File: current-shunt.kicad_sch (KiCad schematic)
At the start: 22 parts, among them J1 Conn_01x02, U1 TSR_1-2450

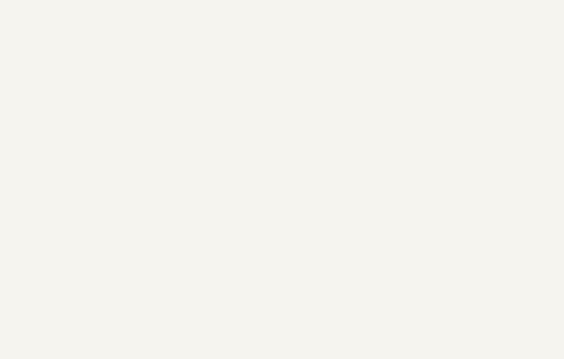
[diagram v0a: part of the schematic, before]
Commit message: Add License to repo and board
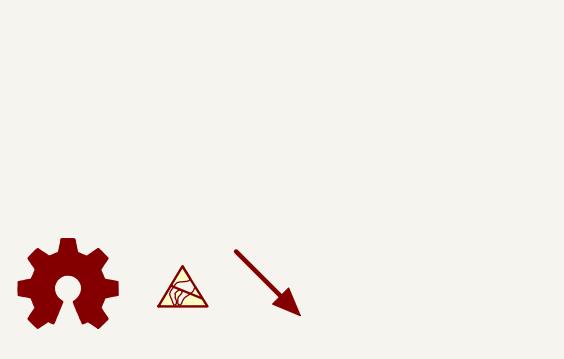
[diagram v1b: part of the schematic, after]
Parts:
- added LOGO1: Logo_Open_Hardware_Small, Symbol:OSHW-Logo2_14.6x12mm_SilkScreen, symbol Graphic:Logo_Open_Hardware_Small
- added LOGO2: SYM_ESD_Small, Symbol:ESD-Logo_6.6x6mm_SilkScreen, symbol Graphic:SYM_ESD_Small
- added LOGO3: SYM_Arrow45_XLarge, Symbol:KiCad-Logo2_5mm_SilkScreen, symbol Graphic:SYM_Arrow45_XLarge
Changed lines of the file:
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@@
     (pin "2")
+  )
+  (symbol (lib_id "Graphic:SYM_ESD_Small") (at 36.83 186.055 0) (unit 1)
+    (in_bom yes) (on_board yes) (fields_autoplaced)
+    (property "Reference" "LOGO2" (id 0) (at 36.83 182.499 0)
+      (effects (font (size 1.27 1.27)) hide)
+    )
+    (property "Value" "SYM_ESD_Small" (id 1) (at 36.83 189.23 0)
+      (effects (font (size 1.27 1.27)) hide)
+    )
+    (property "Footprint" "Symbol:ESD-Logo_6.6x6mm_SilkScreen" (id 2) (at 36.83 185.801 0)
+      (effects (font (size 1.27 1.27)) hide)
+    )
+    (property "Datasheet" "~" (id 3) (at 36.83 185.801 0)
+      (effects (font (size 1.27 1.27)) hide)
+    )
   )
   (symbol (lib_id "power:GND") (at 166.37 170.18 0) (unit 1)
@@
     (pin "1")
   )
+  (symbol (lib_id "Graphic:SYM_Arrow45_XLarge") (at 46.355 185.42 0) (unit 1)
+    (in_bom yes) (on_board yes) (fields_autoplaced)
+    (property "Reference" "LOGO3" (id 0) (at 49.149 182.88 0)
+      (effects (font (size 1.27 1.27)) hide)
+    )
+    (property "Value" "SYM_Arrow45_XLarge" (id 1) (at 46.355 189.992 0)
+      (effects (font (size 1.27 1.27)) hide)
+    )
+    (property "Footprint" "Symbol:KiCad-Logo2_5mm_SilkScreen" (id 2) (at 46.355 185.42 0)
+      (effects (font (size 1.27 1.27)) hide)
+    )
+    (property "Datasheet" "~" (id 3) (at 46.355 185.42 0)
+      (effects (font (size 1.27 1.27)) hide)
+    )
+  )
   (symbol (lib_id "power:PWR_FLAG") (at 115.57 146.05 180) (unit 1)
     (in_bom yes) (on_board yes) (fields_autoplaced)
@@
     )
     (pin "1")
+  )
+  (symbol (lib_id "Graphic:Logo_Open_Hardware_Small") (at 24.13 186.055 0) (unit 1)
+    (in_bom yes) (on_board yes) (fields_autoplaced)
+    (property "Reference" "LOGO1" (id 0) (at 24.13 179.07 0)
+      (effects (font (size 1.27 1.27)) hide)
+    )
+    (property "Value" "Logo_Open_Hardware_Small" (id 1) (at 24.13 191.77 0)
+      (effects (font (size 1.27 1.27)) hide)
+    )
+    (property "Footprint" "Symbol:OSHW-Logo2_14.6x12mm_SilkScreen" (id 2) (at 24.13 186.055 0)
+      (effects (font (size 1.27 1.27)) hide)
+    )
+    (property "Datasheet" "~" (id 3) (at 24.13 186.055 0)
+      (effects (font (size 1.27 1.27)) hide)
+    )
   )
   (symbol (lib_id "Device:D_TVS") (at 143.51 139.7 90) (unit 1)
@@
       (reference "L1") (unit 1) (value "TCK-047") (footprint "Inductor_SMD:L_TracoPower_TCK-047_5.2x5.8mm")
     )
+    (path "/f2ce763b-2f7b-4275-a3f0-c094eb5a3dca"
+      (reference "LOGO1") (unit 1) (value "Logo_Open_Hardware_Small") (footprint "Symbol:OSHW-Logo2_14.6x12mm_SilkScreen")
+    )
+    (path "/4b1c03ec-3982-4499-a628-b0dcacc15186"
+      (reference "LOGO2") (unit 1) (value "SYM_ESD_Small") (footprint "Symbol:ESD-Logo_6.6x6mm_SilkScreen")
+    )
+    (path "/b637814e-8794-4085-8d9d-bf82cbec03bb"
+      (reference "LOGO3") (unit 1) (value "SYM_Arrow45_XLarge") (footprint "Symbol:KiCad-Logo2_5mm_SilkScreen")
+    )
     (path "/9c0976a5-f693-48ee-8912-3bc4f69281a3"

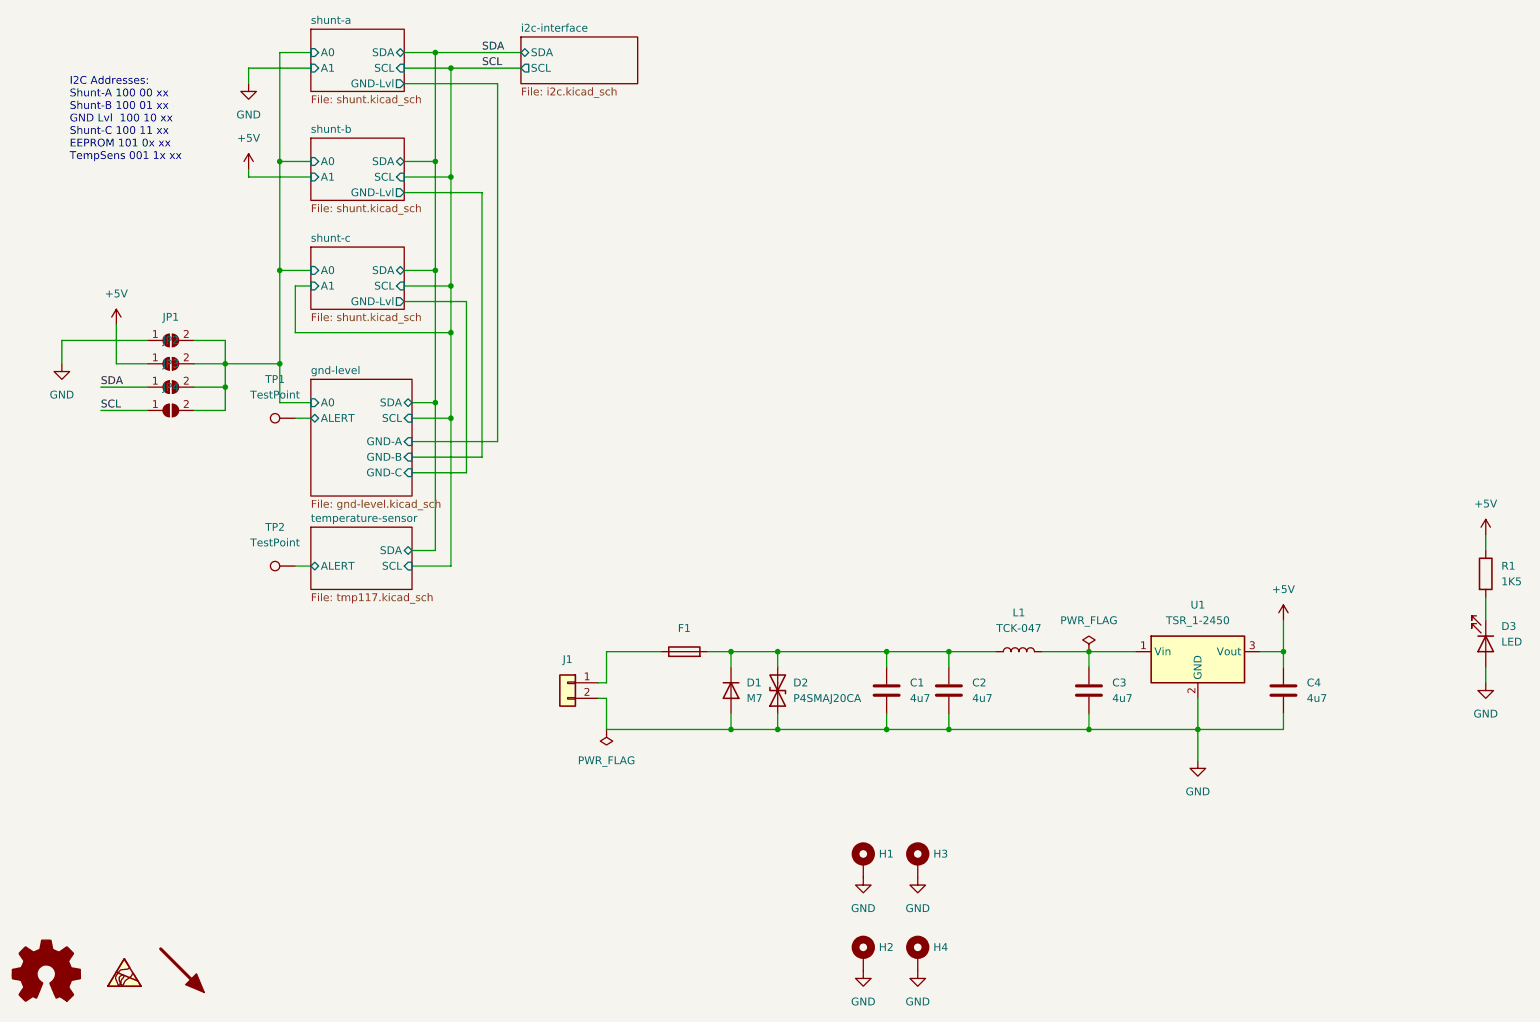
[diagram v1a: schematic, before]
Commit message: Add a lot of nice to haves
* Jumpers to bridge isolation
* I2C pullups with jumpers for input
* Labels on input connectors
* Geographic reference counts
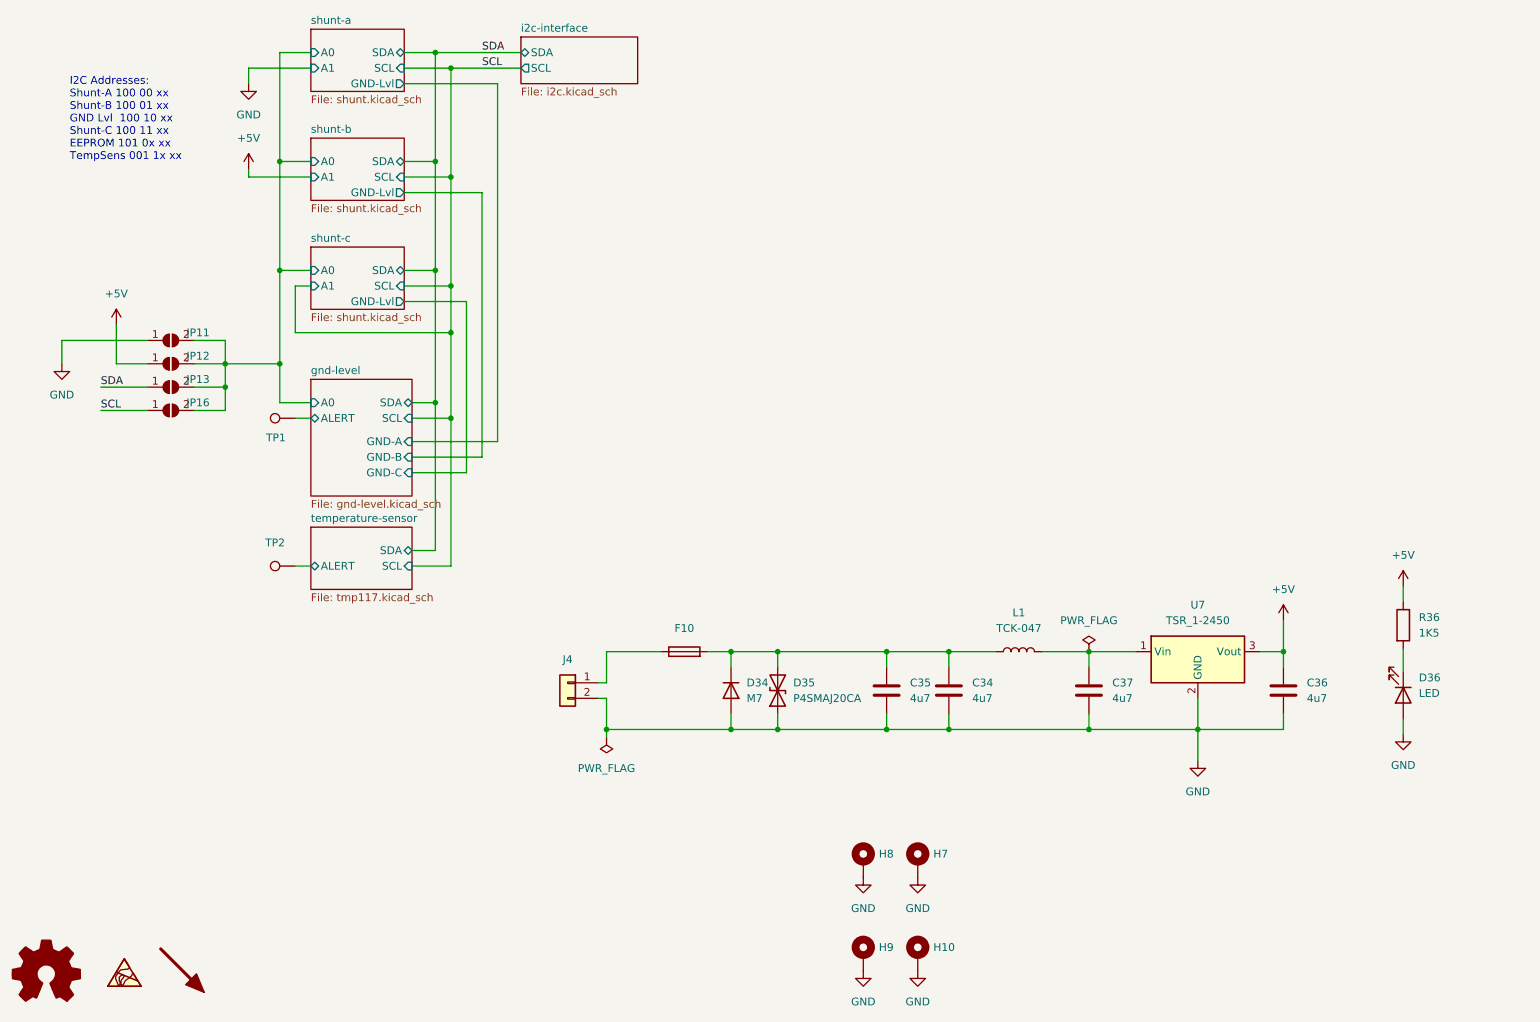
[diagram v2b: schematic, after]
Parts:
- LOGO1: now left out of the parts list
- LOGO2: renamed from LOGO3; now left out of the parts list
- LOGO3: renamed from LOGO2; now left out of the parts list
- renumbered C2 to C34, C1 to C35, C4 to C36, C3 to C37, D1 to D34, D2 to D35, D3 to D36, F1 to F10, H4 to H10, H3 to H7, H1 to H8, H2 to H9, J1 to J4, JP1 to JP11, JP2 to JP12, JP3 to JP13, JP4 to JP16, R1 to R36, U1 to U7
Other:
- moved on the sheet: D36, R36

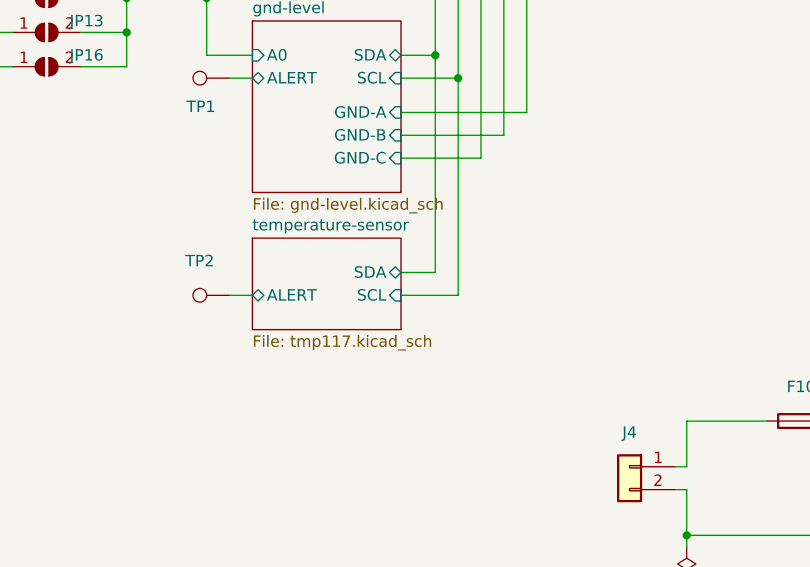
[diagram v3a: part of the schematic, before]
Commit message: Update sheetname to match new use
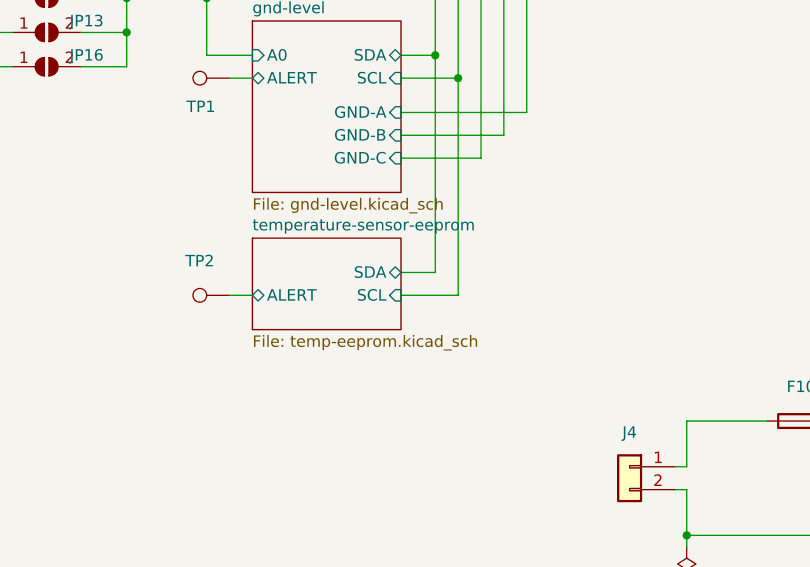
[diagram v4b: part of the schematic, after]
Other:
- sheet temperature-sensor renamed temperature-sensor-eeprom
- sheet temperature-sensor-eeprom: file tmp117.kicad_sch -> temp-eeprom.kicad_sch
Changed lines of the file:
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@@
     (stroke (width 0.1524) (type solid) (color 0 0 0 0))
     (fill (color 0 0 0 0.0000))
-    (property "Sheet name" "temperature-sensor" (id 0) (at 67.31 112.3184 0)
+    (property "Sheet name" "temperature-sensor-eeprom" (id 0) (at 67.31 112.3184 0)
       (effects (font (size 1.27 1.27)) (justify left bottom))
     )
-    (property "Sheet file" "tmp117.kicad_sch" (id 1) (at 67.31 123.7746 0)
+    (property "Sheet file" "temp-eeprom.kicad_sch" (id 1) (at 67.31 123.7746 0)
       (effects (font (size 1.27 1.27)) (justify left top))
     )
@@
       (reference "#PWR096") (unit 1) (value "GND") (footprint "")
     )
-    (path "/33599c98-c878-4908-a7c6-678a8ce7a2a3/d0396036-0f65-40f9-92a3-4919f6979ac2"
-      (reference "#PWR097") (unit 1) (value "+5V") (footprint "")
-    )
-    (path "/33599c98-c878-4908-a7c6-678a8ce7a2a3/4706ea93-88f3-4880-9015-7e9e4dcf0f5a"
-      (reference "#PWR098") (unit 1) (value "GND") (footprint "")
-    )
-    (path "/33599c98-c878-4908-a7c6-678a8ce7a2a3/6dea175e-2c41-4ac4-b283-0414d4c249e9"
-      (reference "#PWR099") (unit 1) (value "+5V") (footprint "")
-    )
-    (path "/33599c98-c878-4908-a7c6-678a8ce7a2a3/ecac5dc8-a0f8-4c7a-9d00-87bef52ecc6f"
-      (reference "#PWR0100") (unit 1) (value "GND") (footprint "")
-    )
-    (path "/33599c98-c878-4908-a7c6-678a8ce7a2a3/7bf28146-6685-47c2-b71e-ee157f49f704"
-      (reference "#PWR0101") (unit 1) (value "+5V") (footprint "")
-    )
-    (path "/33599c98-c878-4908-a7c6-678a8ce7a2a3/d342878a-cff6-449d-afad-8c25fd252678"
-      (reference "#PWR0102") (unit 1) (value "GND") (footprint "")
-    )
-    (path "/33599c98-c878-4908-a7c6-678a8ce7a2a3/5c7882c1-5e72-4872-95a8-44f9c88b0af8"
-      (reference "#PWR0103") (unit 1) (value "+5V") (footprint "")
-    )
-    (path "/33599c98-c878-4908-a7c6-678a8ce7a2a3/0a1ed228-2770-4052-a4bd-6f8cea40e322"
-      (reference "#PWR0104") (unit 1) (value "GND") (footprint "")
-    )
-    (path "/33599c98-c878-4908-a7c6-678a8ce7a2a3/0b1a0797-626f-43c3-9c86-4759b6c72390"
-      (reference "#PWR0105") (unit 1) (value "+5V") (footprint "")
-    )
-    (path "/33599c98-c878-4908-a7c6-678a8ce7a2a3/233b6c4e-89fa-49a5-94e1-32c2bfea7912"
-      (reference "#PWR0106") (unit 1) (value "GND") (footprint "")
-    )
-    (path "/33599c98-c878-4908-a7c6-678a8ce7a2a3/74413d50-fc28-44a8-8dc9-1fffb6bdf867"
-      (reference "#PWR0107") (unit 1) (value "+5V") (footprint "")
-    )
-    (path "/33599c98-c878-4908-a7c6-678a8ce7a2a3/c30bd523-3d0d-477b-ab45-7b5ac95bea9c"
-      (reference "#PWR0108") (unit 1) (value "GND") (footprint "")
-    )
-    (path "/33599c98-c878-4908-a7c6-678a8ce7a2a3/28d81186-3c14-4508-88e5-c295f1178312"
-      (reference "#PWR0109") (unit 1) (value "+5V") (footprint "")
-    )
-    (path "/33599c98-c878-4908-a7c6-678a8ce7a2a3/9708efb8-f31a-4285-bcd0-cf48b0277122"
-      (reference "#PWR0110") (unit 1) (value "GND") (footprint "")
-    )
-    (path "/33599c98-c878-4908-a7c6-678a8ce7a2a3/f7024409-6b56-4142-8775-cff64567c0f6"
-      (reference "#PWR0111") (unit 1) (value "+5V") (footprint "")
-    )
-    (path "/33599c98-c878-4908-a7c6-678a8ce7a2a3/b2477d6b-d121-4799-b90a-4337cc4ef6d1"
-      (reference "#PWR0112") (unit 1) (value "GND") (footprint "")
-    )
     (path "/99003ed3-c5d1-4f7d-aaa6-65dc5647b7c4/8606e9a7-b6bf-435f-a22e-1141583f01b6"
       (reference "#PWR0113") (unit 1) (value "+5V") (footprint "")
@@
       (reference "#PWR0118") (unit 1) (value "GND") (footprint "")
     )
+    (path "/33599c98-c878-4908-a7c6-678a8ce7a2a3/0a1ed228-2770-4052-a4bd-6f8cea40e322"
+      (reference "#PWR?") (unit 1) (value "GND") (footprint "")
+    )
+    (path "/33599c98-c878-4908-a7c6-678a8ce7a2a3/0b1a0797-626f-43c3-9c86-4759b6c72390"
+      (reference "#PWR?") (unit 1) (value "+5V") (footprint "")
+    )
+    (path "/33599c98-c878-4908-a7c6-678a8ce7a2a3/233b6c4e-89fa-49a5-94e1-32c2bfea7912"
+      (reference "#PWR?") (unit 1) (value "GND") (footprint "")
+    )
+    (path "/33599c98-c878-4908-a7c6-678a8ce7a2a3/28d81186-3c14-4508-88e5-c295f1178312"
+      (reference "#PWR?") (unit 1) (value "+5V") (footprint "")
+    )
+    (path "/33599c98-c878-4908-a7c6-678a8ce7a2a3/4706ea93-88f3-4880-9015-7e9e4dcf0f5a"
+      (reference "#PWR?") (unit 1) (value "GND") (footprint "")
+    )
+    (path "/33599c98-c878-4908-a7c6-678a8ce7a2a3/5c7882c1-5e72-4872-95a8-44f9c88b0af8"
+      (reference "#PWR?") (unit 1) (value "+5V") (footprint "")
+    )
+    (path "/33599c98-c878-4908-a7c6-678a8ce7a2a3/6dea175e-2c41-4ac4-b283-0414d4c249e9"
+      (reference "#PWR?") (unit 1) (value "+5V") (footprint "")
+    )
+    (path "/33599c98-c878-4908-a7c6-678a8ce7a2a3/74413d50-fc28-44a8-8dc9-1fffb6bdf867"
+      (reference "#PWR?") (unit 1) (value "+5V") (footprint "")
+    )
+    (path "/33599c98-c878-4908-a7c6-678a8ce7a2a3/7bf28146-6685-47c2-b71e-ee157f49f704"
+      (reference "#PWR?") (unit 1) (value "+5V") (footprint "")
+    )
+    (path "/33599c98-c878-4908-a7c6-678a8ce7a2a3/9708efb8-f31a-4285-bcd0-cf48b0277122"
+      (reference "#PWR?") (unit 1) (value "GND") (footprint "")
+    )
+    (path "/33599c98-c878-4908-a7c6-678a8ce7a2a3/b2477d6b-d121-4799-b90a-4337cc4ef6d1"
+      (reference "#PWR?") (unit 1) (value "GND") (footprint "")
+    )
+    (path "/33599c98-c878-4908-a7c6-678a8ce7a2a3/c30bd523-3d0d-477b-ab45-7b5ac95bea9c"
+      (reference "#PWR?") (unit 1) (value "GND") (footprint "")
+    )
+    (path "/33599c98-c878-4908-a7c6-678a8ce7a2a3/d0396036-0f65-40f9-92a3-4919f6979ac2"
+      (reference "#PWR?") (unit 1) (value "+5V") (footprint "")
+    )
+    (path "/33599c98-c878-4908-a7c6-678a8ce7a2a3/d342878a-cff6-449d-afad-8c25fd252678"
+      (reference "#PWR?") (unit 1) (value "GND") (footprint "")
+    )
+    (path "/33599c98-c878-4908-a7c6-678a8ce7a2a3/ecac5dc8-a0f8-4c7a-9d00-87bef52ecc6f"
+      (reference "#PWR?") (unit 1) (value "GND") (footprint "")
+    )
+    (path "/33599c98-c878-4908-a7c6-678a8ce7a2a3/f7024409-6b56-4142-8775-cff64567c0f6"
+      (reference "#PWR?") (unit 1) (value "+5V") (footprint "")
+    )
     (path "/d6b46817-7c60-4479-a350-904d72633f16/2f8940a3-0c62-4374-a8eb-13bed970a1a2"

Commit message: Add LCSC order numbers to more easily order at JLCPCB
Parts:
- C34, C35, C36, C37: LCSC Part # (none) -> C29823
- D34: LCSC Part # (none) -> C95872
- D35: LCSC Part # (none) -> C391567
- D36: LCSC Part # (none) -> C2286
- F10: value Fuse_Small -> 1206L016WR; LCSC Part # (none) -> C151161
- H10, H7, H8, H9, TP1, TP2: now left out of the parts list
- R36: LCSC Part # (none) -> C22843

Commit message: Remove PCB only parts from BOM
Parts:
- JP11, JP12, JP13, JP16: now left out of the parts list
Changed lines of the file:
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@@
   )
   (symbol (lib_id "Jumper:SolderJumper_2_Open") (at 44.45 93.98 0) (unit 1)
-    (in_bom yes) (on_board yes)
+    (in_bom no) (on_board yes)
     (property "Reference" "JP16" (id 0) (at 48.895 92.71 0))
     (property "Value" "SolderJumper_2_Open" (id 1) (at 43.1801 96.52 90)
@@
   )
   (symbol (lib_id "Jumper:SolderJumper_2_Open") (at 44.45 90.17 0) (unit 1)
-    (in_bom yes) (on_board yes)
+    (in_bom no) (on_board yes)
     (property "Reference" "JP13" (id 0) (at 48.895 88.9 0))
     (property "Value" "SolderJumper_2_Open" (id 1) (at 43.1801 92.71 90)
@@
   )
   (symbol (lib_id "Jumper:SolderJumper_2_Open") (at 44.45 82.55 0) (unit 1)
-    (in_bom yes) (on_board yes)
+    (in_bom no) (on_board yes)
     (property "Reference" "JP11" (id 0) (at 48.895 81.28 0))
     (property "Value" "SolderJumper_2_Open" (id 1) (at 43.1801 85.09 90)
@@
   )
   (symbol (lib_id "Jumper:SolderJumper_2_Open") (at 44.45 86.36 0) (unit 1)
-    (in_bom yes) (on_board yes)
+    (in_bom no) (on_board yes)
     (property "Reference" "JP12" (id 0) (at 48.895 85.09 0))
     (property "Value" "SolderJumper_2_Open" (id 1) (at 43.1801 88.9 90)

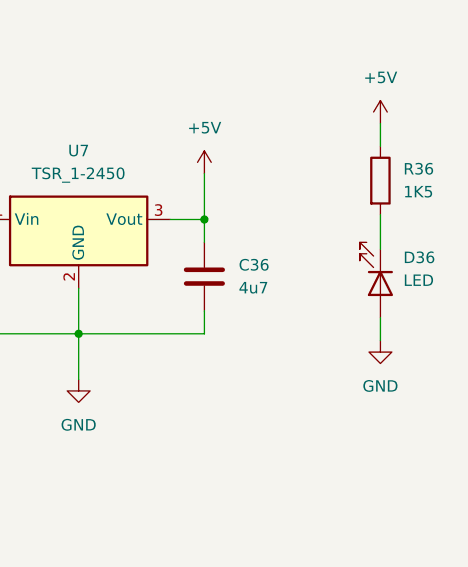
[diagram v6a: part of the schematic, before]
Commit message: Add JLCPCB rotation offsets
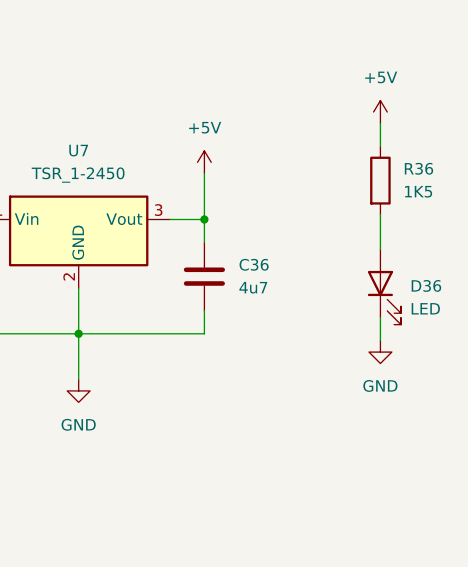
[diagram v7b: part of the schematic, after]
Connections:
- net GND: now also D36.1 (K); no longer D36.2 (A)
- net at R36.2: now also D36.2 (A); no longer D36.1 (K)
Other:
- moved on the sheet: D36
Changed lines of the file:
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@@
     (pin "1")
   )
-  (symbol (lib_id "Device:LED") (at 245.618 140.462 270) (unit 1)
+  (symbol (lib_id "Device:LED") (at 245.618 140.462 90) (unit 1)
     (in_bom yes) (on_board yes) (fields_autoplaced)
-    (property "Reference" "D36" (id 0) (at 248.158 137.6044 90)
-      (effects (font (size 1.27 1.27)) (justify left))
+    (property "Reference" "D36" (id 0) (at 248.92 140.7794 90)
+      (effects (font (size 1.27 1.27)) (justify right))
     )
-    (property "Value" "LED" (id 1) (at 248.158 140.1444 90)
-      (effects (font (size 1.27 1.27)) (justify left))
+    (property "Value" "LED" (id 1) (at 248.92 143.3194 90)
+      (effects (font (size 1.27 1.27)) (justify right))
     )
     (property "Footprint" "LED_SMD:LED_0603_1608Metric" (id 2) (at 245.618 140.462 0)
